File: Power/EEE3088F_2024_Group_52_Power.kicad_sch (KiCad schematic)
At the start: 29 parts, among them J1 Conn_02x08_Odd_Even, J2 Conn_01x02, Q1 AO3401A, SW1 MINI MSK12CO2, U1 LMV321IDBVR, U2 TP4056, U3 DRV8837CDSGR, U4 DRV8837CDSGR

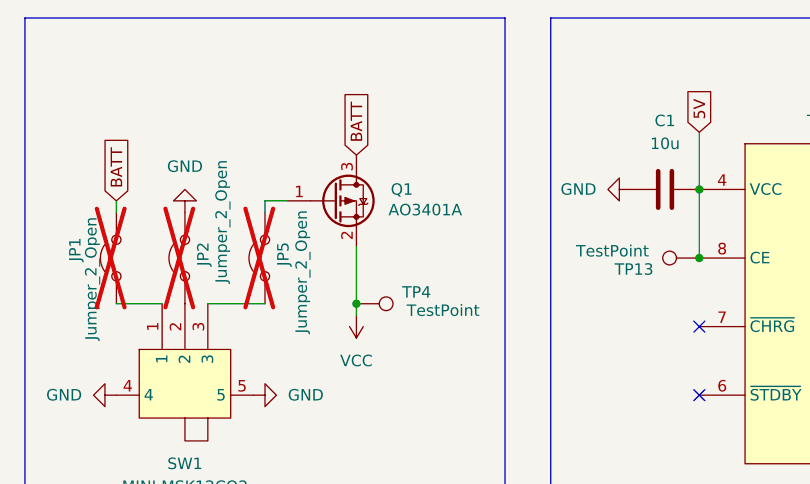
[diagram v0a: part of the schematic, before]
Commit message: Proposed fixes to power PCB flaws
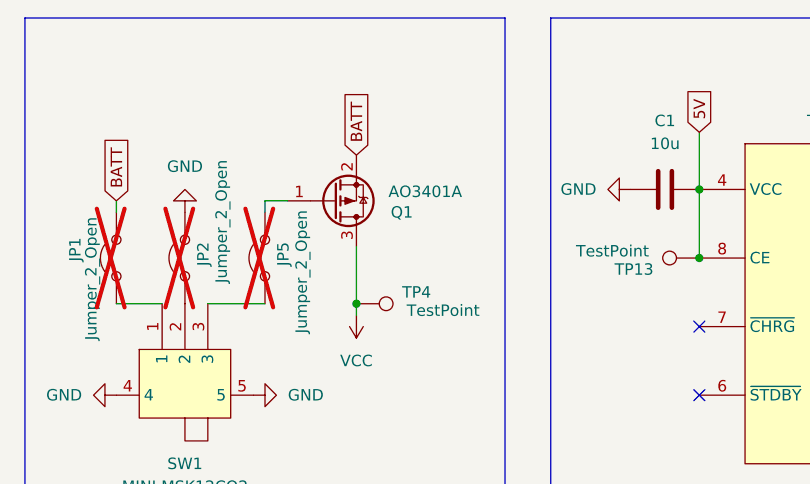
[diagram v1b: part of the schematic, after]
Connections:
- net BATT: now also Q1.2 (S); no longer Q1.3 (D)
- net VCC: now also Q1.3 (D); no longer Q1.2 (S)
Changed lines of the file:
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@@
 		(title "EEE3088F 2024 Group 52 Power")
 		(date "2024-03-23")
-		(rev "v0")
+		(rev "v1")
 		(comment 3 "NDXTRI021")
 		(comment 4 "Triss Naidoo")
@@
 		(lib_id "Transistor_FET:AO3401A")
 		(at 186.69 35.56 0)
+		(mirror x)
 		(unit 1)
 		(exclude_from_sim no)
@@
 		(dnp no)
 		(property "Reference" "Q1"
-			(at 193.04 34.2899 0)
+			(at 193.04 36.8301 0)
 			(effects
 				(font
@@
 		)
 		(property "Value" "AO3401A"
-			(at 192.786 36.576 0)
+			(at 192.786 34.544 0)
 			(effects
 				(font
@@
 		)
 		(property "Footprint" "Easy2Ki_Library:SOT-23_L2.9-W1.3-P1.90-LS2.4-BR"
-			(at 191.77 37.465 0)
+			(at 191.77 33.655 0)
 			(effects
 				(font
@@
 		)
 		(property "Datasheet" "http://www.aosmd.com/pdfs/datasheet/AO3401A.pdf"
-			(at 191.77 39.37 0)
+			(at 191.77 31.75 0)
 			(effects
 				(font
